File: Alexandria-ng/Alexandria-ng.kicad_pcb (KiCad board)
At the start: 4 copper layers, 87 parts, among them J1 Eth0, J10 PoE3, J11 PoE4, J12 FFC, J13 +3.3V, J14 I²C, J2 Eth1, J3 Eth2, J4 Eth3, J5 Eth4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

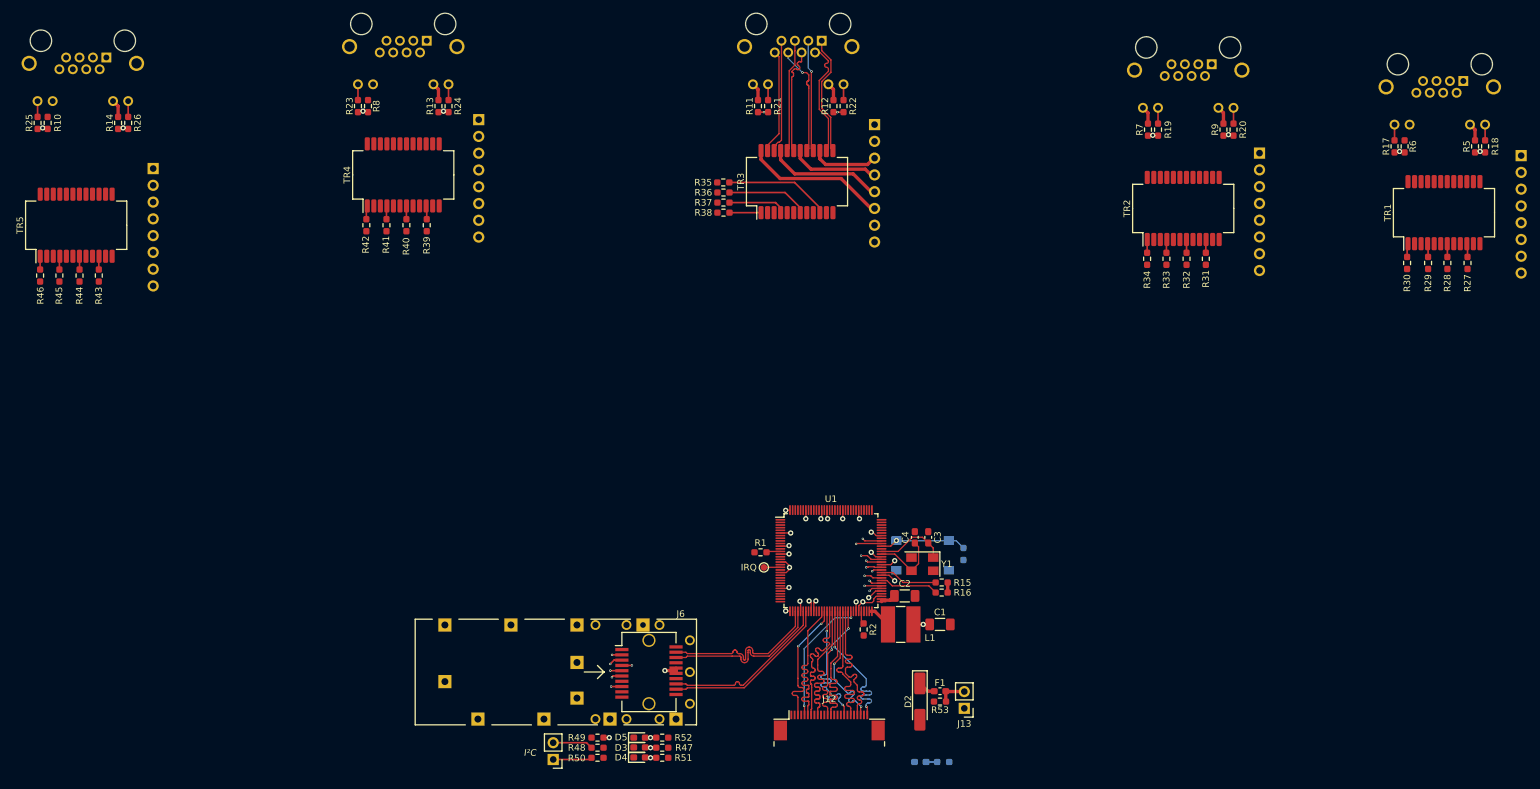
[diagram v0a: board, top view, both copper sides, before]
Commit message: Finally routed Ethernet pairs, added power rail fills under the IC
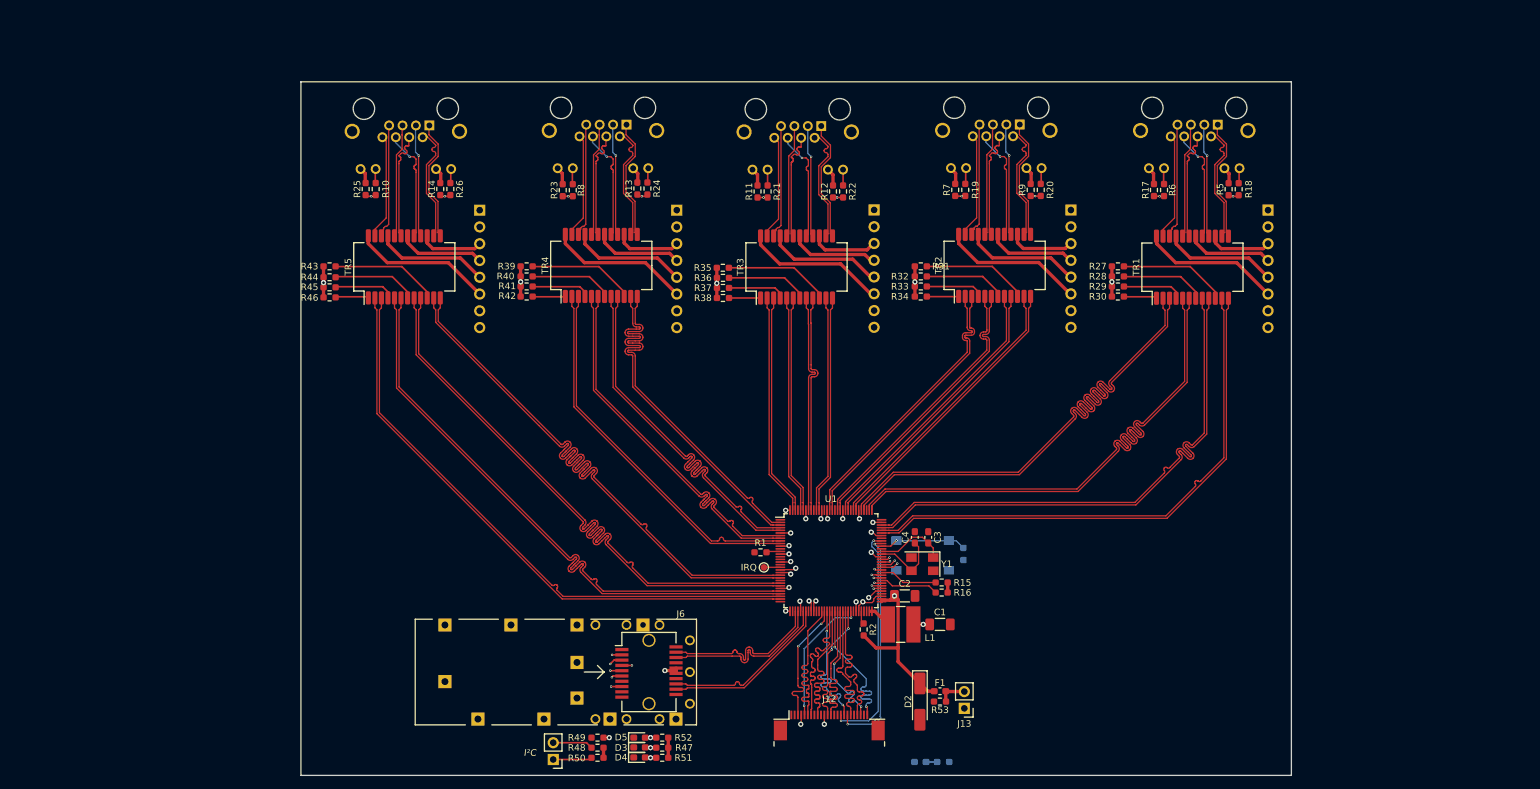
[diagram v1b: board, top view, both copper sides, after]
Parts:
- moved R27 52.9 mm to (195.9, 67.2), turned to 180 degrees
- moved R10 50.7 mm to (83.5, 55.5)
- moved R25 50.7 mm to (81.9, 55.5)
- moved TR5 50.1 mm to (87.8, 67.3)
- moved J5 50.0 mm to (91.6, 45.9)
- moved R28 49.9 mm to (195.9, 68.7), turned to 180 degrees
- moved J11 49.8 mm to (99.2, 58.7)
- moved R26 49.8 mm to (94.8, 55.5)
- moved R14 49.8 mm to (93.2, 55.5)
- moved R29 47.1 mm to (195.9, 70.2), turned to 180 degrees
- moved R30 44.1 mm to (195.9, 71.8), turned to 180 degrees
- moved R46 44.0 mm to (76.5, 71.9), turned to 180 degrees
- moved R31 43.2 mm to (166.0, 67.2), turned to 0 degrees
- moved R45 41.0 mm to (76.5, 70.4), turned to 180 degrees
- moved R32 40.3 mm to (166.0, 68.7), turned to 180 degrees
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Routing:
- net E4DN: track 0.00 -> 90.4 mm
- net E4DP: track 0.00 -> 90.3 mm
- net E4CN: track 0.00 -> 90.3 mm
- net E4CP: track 0.00 -> 90.2 mm
- net E4BN: track 0.00 -> 90.2 mm
- net E4BP: track 0.00 -> 90.1 mm
- net E4AN: track 0.00 -> 90.1 mm
- net E4AP: track 0.00 -> 90.1 mm
- net E0AP: track 0.00 -> 81.3 mm
- net E0AN: track 0.00 -> 81.3 mm
- net E0BP: track 0.00 -> 81.2 mm
- net E0BN: track 0.00 -> 81.2 mm
- net E0CN: track 0.00 -> 81.1 mm
- net E0CP: track 0.00 -> 81.1 mm
- net E0DP: track 0.00 -> 81.0 mm
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- added copper zone on In1.Cu, net +1V1
- added copper zone on In2.Cu, net +3.3V
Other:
- board outline added: 150 x 105 mm
- board text added: "+1.1V fill"
- board text added: "+3.3V fill"
- board text added: "-- Magnetics <-> Jack -- Worst intra-pair skew: 415.9 µm (A pair) Allowed in total: 50 mil (1270 µm) Worst inter-pair skew: 2635.5 µm (DN-AP) Allowed in total: 600 mil (15240 µm) Source: https://ww1.microchip.com/downloads/en/Appnotes/00002054A.pdf"
- board text removed: "Worst intra-pair skew: 415.9 µm (A pair) Allowed in total: 50 mil (1270 µm) Worst inter-pair skew: 2635.5 µm (DN-AP) Allowed in total: 600 mil (15240 µm) Source: https://ww1.microchip.com/downloads/en/Appnotes/00002054A.pdf"

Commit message: Power routing
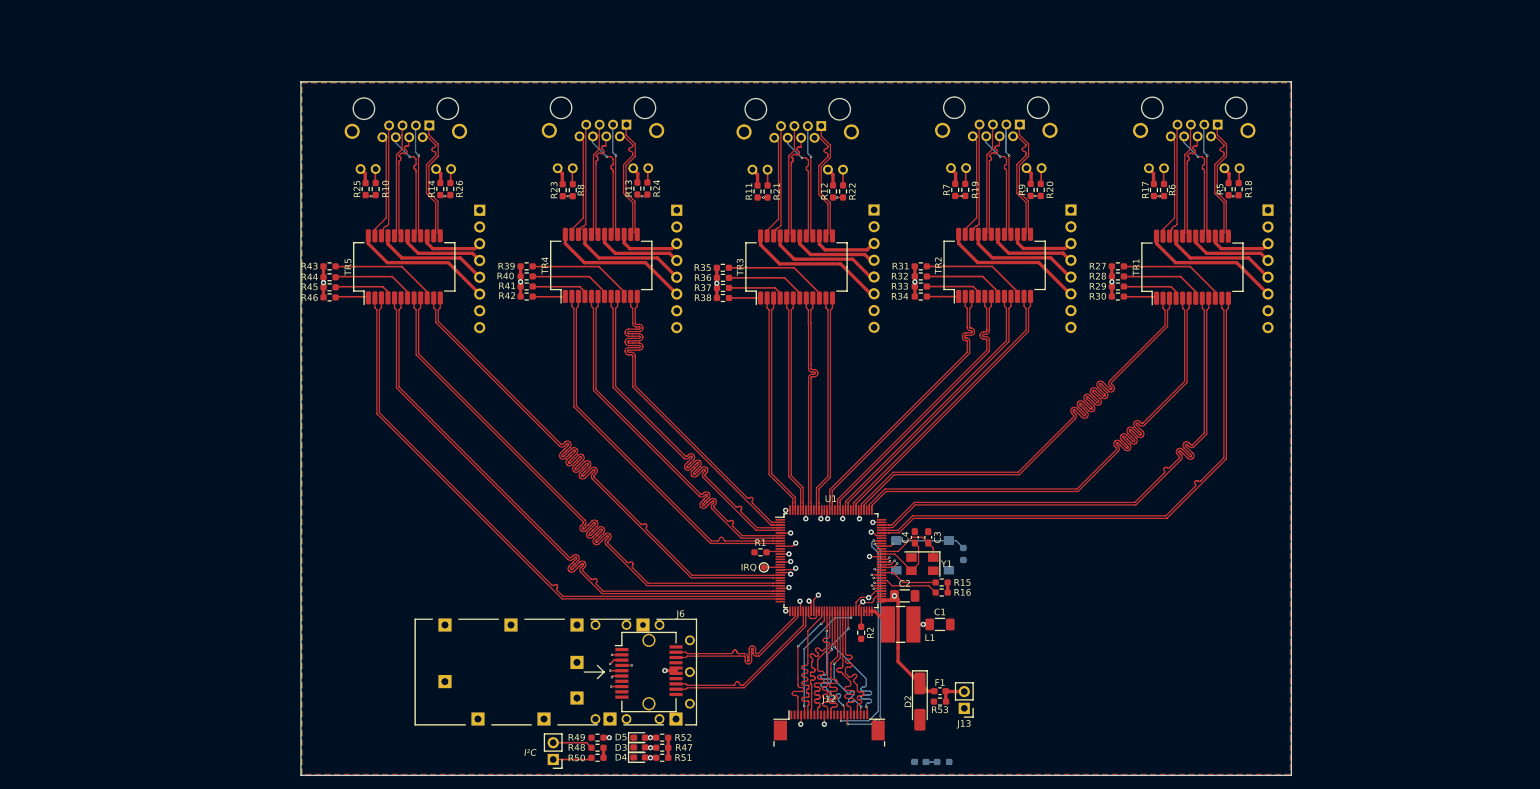
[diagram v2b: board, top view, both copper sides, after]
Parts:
- moved R2 0.63 mm to (157.0, 122.7)
- turned R31 to 180 degrees
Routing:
- net +3.3V: track 73.5 -> 68.6 mm
- net GND: track 7.18 -> 11.1 mm
- net +1V1: track 30.1 -> 32.2 mm, vias 12 -> 11
- net +2V8: track 30.0 -> 31.3 mm
- net RSTn: track 13.1 -> 12.4 mm
- added copper zone on B.Cu, net GND
- added copper zone on F.Cu, net GND
- added copper zone on In2.Cu, net GND

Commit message: More power routing
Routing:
- net +2V8: track 31.3 -> 85.7 mm, vias 4 -> 5
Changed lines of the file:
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@@
   (segment (start 212.683039 54.751976) (end 212.683039 53.126476) (width 0.508) (layer "F.Cu") (net 90))
   (segment (start 171.281039 53.102976) (end 170.513039 52.334976) (width 0.508) (layer "F.Cu") (net 90))
+  (segment (start 167.9975 133.096) (end 167.9975 134.8505) (width 0.508) (layer "F.Cu") (net 90))
   (segment (start 141.2795 53.308415) (end 140.5115 52.540415) (width 0.508) (layer "F.Cu") (net 90))
   (segment (start 158.623 118.11) (end 157.353 118.11) (width 0.14986) (layer "F.Cu") (net 90))
   (segment (start 141.2795 54.933915) (end 141.2795 53.308415) (width 0.508) (layer "F.Cu") (net 90))
   (segment (start 147.896 135.114) (end 147.896 136.457) (width 0.14986) (layer "F.Cu") (net 90))
+  (segment (start 167.9975 134.8505) (end 168.021 134.874) (width 0.508) (layer "F.Cu") (net 90))
   (segment (start 158.877 117.530802) (end 158.877 117.856) (width 0.14986) (layer "F.Cu") (net 90))
   (segment (start 151.396 136.525) (end 151.396 135.114) (width 0.14986) (layer "F.Cu") (net 90))
@@
   (segment (start 160.0625 117.16) (end 159.247802 117.16) (width 0.14986) (layer "F.Cu") (net 90))
   (via (at 150.495 116.967) (size 0.8) (drill 0.4) (layers "F.Cu" "B.Cu") (net 90))
+  (via (at 168.021 134.874) (size 0.8) (drill 0.4) (layers "F.Cu" "B.Cu") (net 90))
   (via (at 157.226 117.983) (size 0.8) (drill 0.4) (layers "F.Cu" "B.Cu") (net 90))
   (via (at 151.396 136.525) (size 0.8) (drill 0.4) (layers "F.Cu" "B.Cu") (net 90))
   (via (at 147.828 136.525) (size 0.8) (drill 0.4) (layers "F.Cu" "B.Cu") (net 90))
+  (segment (start 151.396 136.918) (end 152.654 138.176) (width 0.508) (layer "B.Cu") (net 90))
+  (segment (start 147.828 136.525) (end 151.396 136.525) (width 0.508) (layer "B.Cu") (net 90))
+  (segment (start 164.846 138.176) (end 168.021 135.001) (width 0.508) (layer "B.Cu") (net 90))
+  (segment (start 145.034 133.731) (end 147.828 136.525) (width 0.508) (layer "B.Cu") (net 90))
+  (segment (start 150.495 118.237) (end 145.034 123.698) (width 0.508) (layer "B.Cu") (net 90))
+  (segment (start 145.034 123.698) (end 145.034 133.731) (width 0.508) (layer "B.Cu") (net 90))
+  (segment (start 168.021 135.001) (end 168.021 134.874) (width 0.508) (layer "B.Cu") (net 90))
+  (segment (start 157.226 117.983) (end 156.21 116.967) (width 0.508) (layer "B.Cu") (net 90))
+  (segment (start 151.396 136.525) (end 151.396 136.918) (width 0.508) (layer "B.Cu") (net 90))
+  (segment (start 152.654 138.176) (end 164.846 138.176) (width 0.508) (layer "B.Cu") (net 90))
+  (segment (start 156.21 116.967) (end 150.495 116.967) (width 0.508) (layer "B.Cu") (net 90))
+  (segment (start 150.495 116.967) (end 150.495 118.237) (width 0.508) (layer "B.Cu") (net 90))
   (segment (start 155.44943 120.396) (end 155.4 120.34657) (width 0.14986) (layer "F.Cu") (net 91))
   (segment (start 148.396 135.114) (end 148.396 133.791) (width 0.14986) (layer "F.Cu") (net 91))

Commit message: GND improvements
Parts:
- moved R2 2.03 mm to (157.0, 124.7)
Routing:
- net +3.3V: track 68.6 -> 74.2 mm
- net Net-(U1-EN_SWR): track 2.26 -> 4.39 mm
- net GND: track 11.1 -> 12.9 mm, vias 0 -> 6
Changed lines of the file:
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@@
   )
   (footprint "Resistor_SMD:R_0603_1608Metric_Pad0.98x0.95mm_HandSolder" (layer "F.Cu")
-    (at 156.972 122.682 -90)
+    (at 156.972 124.714 -90)
     (descr "Resistor SMD 0603 (1608 Metric), square (rectangular) end terminal, IPC_7351 nominal with elongated pad for handsoldering. (Body size source: IPC-SM-782 page 72, https://www.pcb-3d.com/wordpress/wp-content/uploads/ipc-sm-782a_amendment_1_and_2.pdf), generated with kicad-footprint-generator")
     (tags "resistor handsolder")
@@
   (segment (start 150.2 120.31) (end 150.2 119.4225) (width 0.14986) (layer "F.Cu") (net 2))
   (segment (start 202.777039 54.751976) (end 202.777039 52.360476) (width 0.254) (layer "F.Cu") (net 2))
+  (segment (start 155.8 118.208) (end 155.321 117.729) (width 0.14986) (layer "F.Cu") (net 2))
   (segment (start 202.777039 52.360476) (end 202.775039 52.358476) (width 0.254) (layer "F.Cu") (net 2))
   (segment (start 149.987 120.523) (end 150.2 120.31) (width 0.14986) (layer "F.Cu") (net 2))
@@
   (segment (start 149 120.166487) (end 149.356513 120.523) (width 0.14986) (layer "F.Cu") (net 2))
   (segment (start 157.4 119.4225) (end 157.8 119.4225) (width 0.25) (layer "F.Cu") (net 2))
+  (segment (start 155.8 119.4225) (end 155.8 118.208) (width 0.14986) (layer "F.Cu") (net 2))
   (segment (start 83.397039 54.751976) (end 83.397039 52.360476) (width 0.254) (layer "F.Cu") (net 2))
   (segment (start 150.6 119.4225) (end 150.2 119.4225) (width 0.25) (layer "F.Cu") (net 2))
   (segment (start 83.397039 52.360476) (end 83.395039 52.358476) (width 0.254) (layer "F.Cu") (net 2))
+  (via (at 158.369 121.158) (size 0.8) (drill 0.4) (layers "F.Cu" "B.Cu") (free) (net 2))
+  (via (at 158.369 122.047) (size 0.8) (drill 0.4) (layers "F.Cu" "B.Cu") (free) (net 2))
+  (via (at 158.369 128.397) (size 0.8) (drill 0.4) (layers "F.Cu" "B.Cu") (free) (net 2))
+  (via (at 158.369 122.936) (size 0.8) (drill 0.4) (layers "F.Cu" "B.Cu") (free) (net 2))
+  (via (at 158.369 126.619) (size 0.8) (drill 0.4) (layers "F.Cu" "B.Cu") (free) (net 2))
+  (via (at 158.369 127.508) (size 0.8) (drill 0.4) (layers "F.Cu" "B.Cu") (free) (net 2))
+  (segment (start 156.9955 125.603) (end 156.972 125.6265) (width 0.508) (layer "F.Cu") (net 3))
   (segment (start 165.114539 69.542476) (end 165.114539 71.748476) (width 0.508) (layer "F.Cu") (net 3))
   (segment (start 127.254 128.397) (end 127.127 128.397) (width 0.508) (layer "F.Cu") (net 3))
@@
   (segment (start 105.404739 69.531176) (end 105.404739 71.737176) (width 0.508) (layer "F.Cu") (net 3))
   (segment (start 158.242 111.125) (end 158.277 111.16) (width 0.14986) (layer "F.Cu") (net 3))
+  (segment (start 162.565 125.603) (end 156.9955 125.603) (width 0.508) (layer "F.Cu") (net 3))
   (segment (start 145.542 119.38) (end 145.5845 119.4225) (width 0.14986) (layer "F.Cu") (net 3))
   (segment (start 146.231 111.96) (end 146.304 111.887) (width 0.14986) (layer "F.Cu") (net 3))
-  (segment (start 162.565 127.049) (end 162.565 124.968) (width 0.508) (layer "F.Cu") (net 3))
+  (segment (start 162.565 127.049) (end 162.565 125.603) (width 0.508) (layer "F.Cu") (net 3))
   (segment (start 160.0625 117.739) (end 160.0625 117.96) (width 0.508) (layer "F.Cu") (net 3))
   (segment (start 160.0625 107.96) (end 159.247802 107.96) (width 0.14986) (layer "F.Cu") (net 3))
@@
   (segment (start 156.6 105.292) (end 156.718 105.41) (width 0.14986) (layer "F.Cu") (net 3))
   (segment (start 162.0135 117.094) (end 161.3685 117.739) (width 0.508) (layer "F.Cu") (net 3))
+  (segment (start 162.565 125.603) (end 162.565 124.968) (width 0.508) (layer "F.Cu") (net 3))
   (segment (start 135.113 69.747915) (end 135.113 71.953915) (width 0.508) (layer "F.Cu") (net 3))
   (segment (start 165.114539 71.748476) (end 165.138039 71.771976) (width 0.508) (layer "F.Cu") (net 3))
@@
   (segment (start 144.7375 110.36) (end 142.7745 110.36) (width 0.14986) (layer "F.Cu") (net 109))
   (segment (start 142.7745 110.36) (end 142.6445 110.49) (width 0.14986) (layer "F.Cu") (net 109))
-  (segment (start 156.972 121.666) (end 157 121.638) (width 0.14986) (layer "F.Cu") (net 110))
-  (segment (start 157 121.638) (end 157 119.4225) (width 0.14986) (layer "F.Cu") (net 110))
+  (segment (start 157 119.4225) (end 157 123.7735) (width 0.14986) (layer "F.Cu") (net 110))
+  (segment (start 157 123.7735) (end 156.972 123.8015) (width 0.14986) (layer "F.Cu") (net 110))
   (segment (start 161.458 109.56) (end 160.0625 109.56) (width 0.14986) (layer "F.Cu") (net 111))
   (segment (start 161.798 109.22) (end 161.458 109.56) (width 0.14986) (layer "F.Cu") (net 111))

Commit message: DRC fixes
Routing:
- net +3.3V: track 74.2 -> 190.5 mm, vias 17 -> 20
- net +2V8: track 85.7 -> 110.8 mm, vias 5 -> 6
- net GND: track 12.9 -> 32.3 mm, vias 6 -> 22
- added copper zone on In2.Cu, net +2V8
- added copper zone on B.Cu, net +3.3V
- added copper zone on In1.Cu, net GND

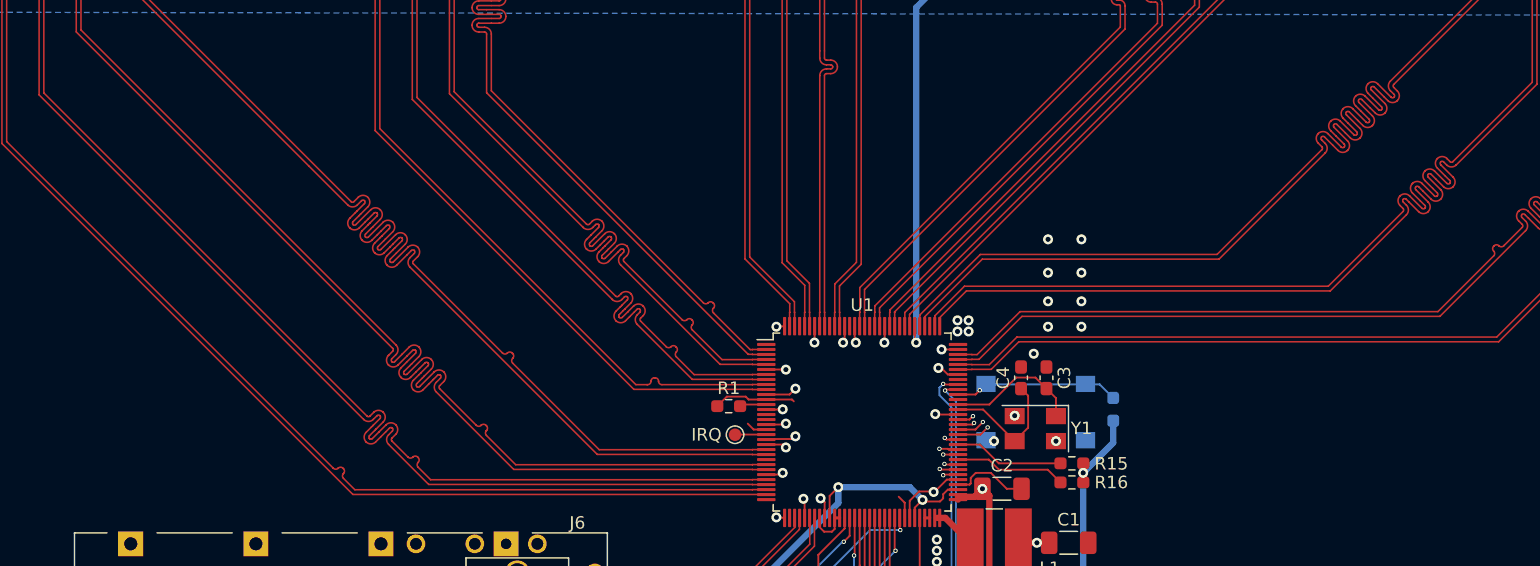
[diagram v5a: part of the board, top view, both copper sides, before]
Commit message: Finally routed all nets
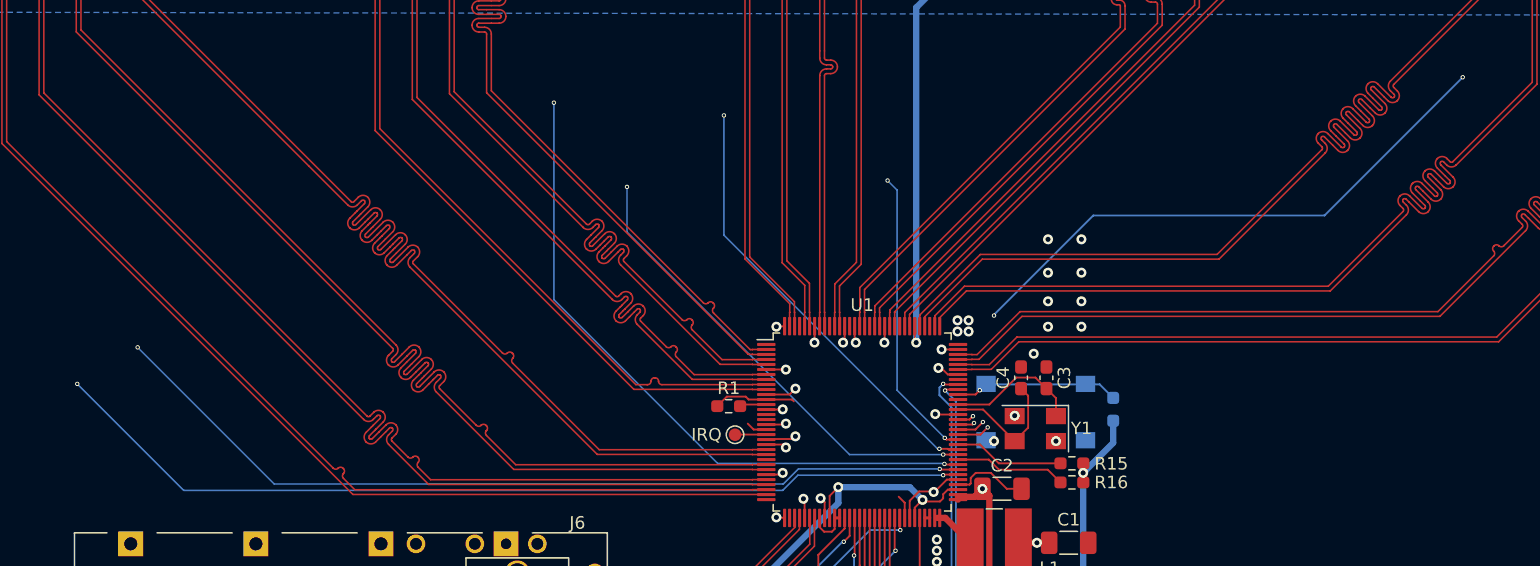
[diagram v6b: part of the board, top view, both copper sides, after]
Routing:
- net P4L0: track 2.73 -> 131.0 mm, vias 2 -> 3
- net P4L1: track 3.01 -> 121.6 mm, vias 2 -> 3
- net P0L1: track 2.85 -> 89.1 mm
- net P3L0: track 2.71 -> 88.9 mm, vias 2 -> 3
- net P3L1: track 2.63 -> 86.5 mm, vias 2 -> 3
- net P0L0: track 2.83 -> 85.3 mm, vias 2 -> 4
- net P2L0: track 3.04 -> 67.7 mm, vias 2 -> 3
- net P1L1: track 4.13 -> 68.4 mm
- net P1L0: track 3.76 -> 63.2 mm
- net P2L1: track 2.64 -> 61.3 mm, vias 2 -> 3
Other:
- board text removed: "+1.1V fill"
- board text removed: "+3.3V fill"
